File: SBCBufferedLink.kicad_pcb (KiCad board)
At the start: 2 copper layers, 9 parts, among them J1 Left, J2 Right

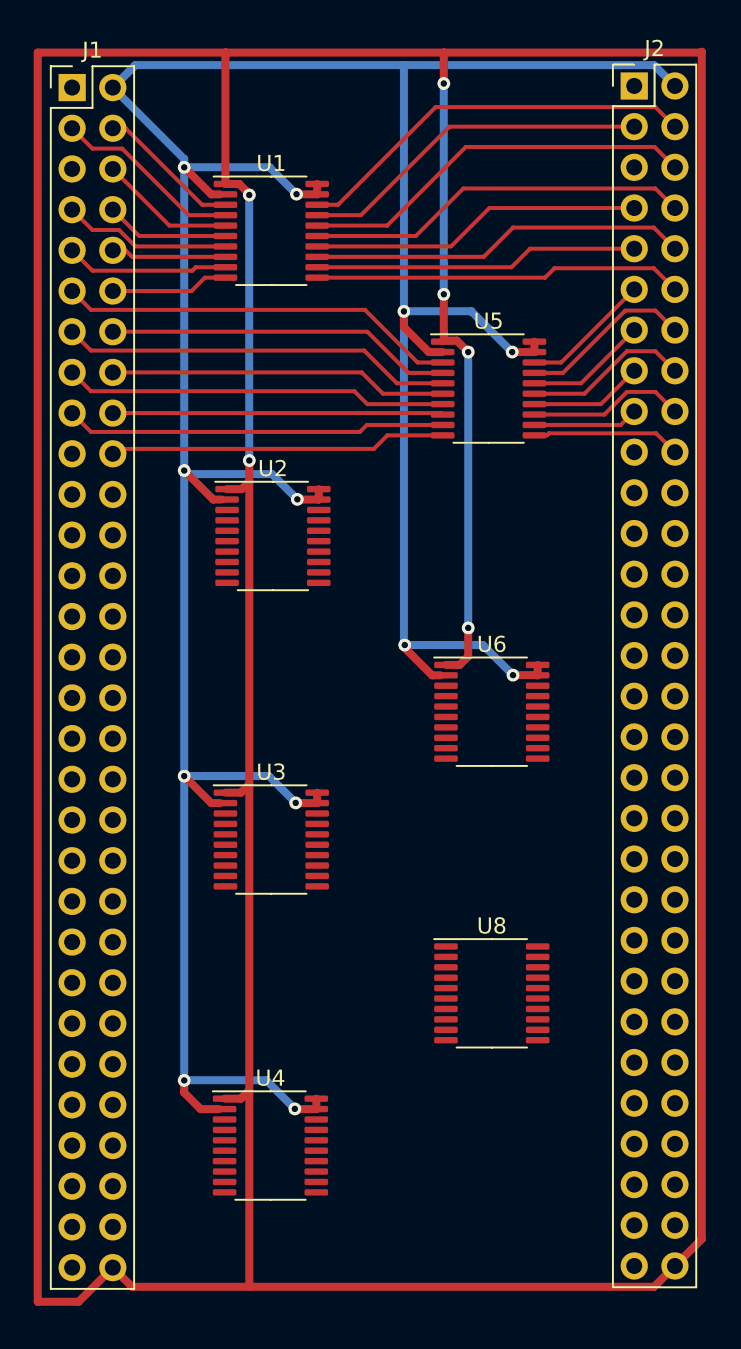
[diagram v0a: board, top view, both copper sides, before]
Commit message: add board edge
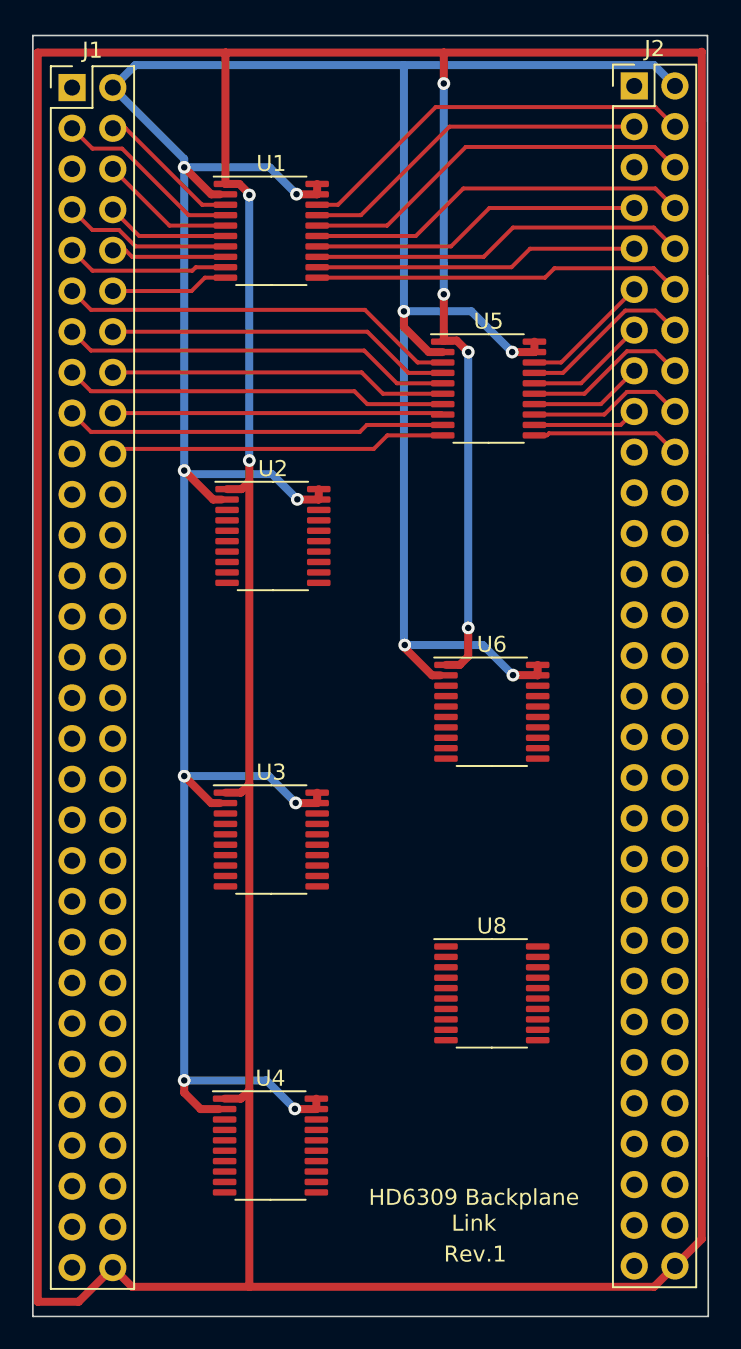
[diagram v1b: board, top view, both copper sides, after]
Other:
- board outline added: 42.2 x 80 mm
- board text added: "HD6309 Backplane Link"
- board text added: "Rev.1"
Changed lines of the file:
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@@
   )
   (paper "A4")
+  (title_block
+    (title "HD6309 SBC Backplane Link")
+    (date "2023-04-24")
+    (rev "Revision 1")
+  )
   (layers
     (0 "F.Cu" signal)
@@
     )
   )
+  (gr_line (start 107.2388 37.7952) (end 149.352 37.7952)
+    (stroke (width 0.1) (type default)) (layer "Edge.Cuts"))
+  (gr_line (start 107.2388 117.7544) (end 107.2388 37.7952)
+    (stroke (width 0.1) (type default)) (layer "Edge.Cuts"))
+  (gr_line (start 149.4028 117.7544) (end 107.2388 117.7544)
+    (stroke (width 0.1) (type default)) (layer "Edge.Cuts"))
+  (gr_line (start 149.352 37.7952) (end 149.4028 117.7544)
+    (stroke (width 0.1) (type default)) (layer "Edge.Cuts"))
   (gr_line (start 107.2896 60.0456) (end 149.7076 60.0456)
     (stroke (width 0.15) (type default)) (layer "User.1"))
@@
   (gr_line (start 122.174 34.544) (end 122.174 121.412)
     (stroke (width 0.15) (type default)) (layer "User.1"))
+  (gr_text "HD6309 Backplane\nLink" (at 134.7724 112.522) (layer "F.SilkS")
+    (effects (font (size 1 1) (thickness 0.15)) (justify bottom))
+  )
+  (gr_text "Rev.1" (at 132.8928 114.4524) (layer "F.SilkS")
+    (effects (font (size 1 1) (thickness 0.15)) (justify left bottom))
+  )
   (segment (start 123.709 47.7122) (end 124.9857 47.7122) (width 0.5) (layer "F.Cu") (net 2))
   (segment (start 118.375 47.7122) (end 118.920751 47.7122) (width 0.5) (layer "F.Cu") (net 2))

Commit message: complete tracing
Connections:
- J1 pad 44: unconnected-(J1-Pin_44-Pad44) -> NC1_LEFT
- J1 pad 53: unconnected-(J1-Pin_53-Pad53) -> NC2_LEFT
- J1 pad 57: unconnected-(J1-Pin_57-Pad57) -> NC3_LEFT
- J1 pad 58: unconnected-(J1-Pin_58-Pad58) -> NC4_LEFT
- J1 pad 59: unconnected-(J1-Pin_59-Pad59) -> NC5_LEFT
- J2 pad 44: unconnected-(J2-Pin_44-Pad44) -> NC1
- J2 pad 53: unconnected-(J2-Pin_53-Pad53) -> NC2
- J2 pad 57: unconnected-(J2-Pin_57-Pad57) -> NC3
- J2 pad 58: unconnected-(J2-Pin_58-Pad58) -> NC4
- J2 pad 59: unconnected-(J2-Pin_59-Pad59) -> NC5
- U2 pad 10: unconnected-(U2-A8-Pad10) -> A8_LEFT
- U2 pad 11: unconnected-(U2-B8-Pad11) -> A8
- U2 pad 12: unconnected-(U2-B7-Pad12) -> D7
- U2 pad 13: unconnected-(U2-B6-Pad13) -> A7
- U2 pad 14: unconnected-(U2-B5-Pad14) -> D6
- U2 pad 15: unconnected-(U2-B4-Pad15) -> A6
- U2 pad 16: unconnected-(U2-B3-Pad16) -> D5
- U2 pad 17: unconnected-(U2-B2-Pad17) -> A5
- U2 pad 18: unconnected-(U2-B1-Pad18) -> D4
- U2 pad 3: unconnected-(U2-A1-Pad3) -> D4_LEFT
- U2 pad 4: unconnected-(U2-A2-Pad4) -> A5_LEFT
- U2 pad 5: unconnected-(U2-A3-Pad5) -> D5_LEFT
- U2 pad 6: unconnected-(U2-A4-Pad6) -> A6_LEFT
- U2 pad 7: unconnected-(U2-A5-Pad7) -> D6_LEFT
- U2 pad 8: unconnected-(U2-A6-Pad8) -> A7_LEFT
- U2 pad 9: unconnected-(U2-A7-Pad9) -> D7_LEFT
- U3 pad 10: unconnected-(U3-A8-Pad10) -> NC1_LEFT
- U3 pad 11: unconnected-(U3-B8-Pad11) -> NC1
- U3 pad 12: unconnected-(U3-B7-Pad12) -> Q6
- U3 pad 13: unconnected-(U3-B6-Pad13) -> A15
- U3 pad 14: unconnected-(U3-B5-Pad14) -> Q5
- U3 pad 15: unconnected-(U3-B4-Pad15) -> A14
- U3 pad 16: unconnected-(U3-B3-Pad16) -> Q4
- U3 pad 17: unconnected-(U3-B2-Pad17) -> A13
- U3 pad 18: unconnected-(U3-B1-Pad18) -> Q3
- U3 pad 3: unconnected-(U3-A1-Pad3) -> Q3_LEFT
- U3 pad 4: unconnected-(U3-A2-Pad4) -> A13_LEFT
- U3 pad 5: unconnected-(U3-A3-Pad5) -> Q4_LEFT
- U3 pad 6: unconnected-(U3-A4-Pad6) -> A14_LEFT
- U3 pad 7: unconnected-(U3-A5-Pad7) -> Q5_LEFT
- U3 pad 8: unconnected-(U3-A6-Pad8) -> A15_LEFT
- U3 pad 9: unconnected-(U3-A7-Pad9) -> Q6_LEFT
- U4 pad 10: unconnected-(U4-A8-Pad10) -> NC5_LEFT
- U4 pad 11: unconnected-(U4-B8-Pad11) -> NC5
- U4 pad 12: unconnected-(U4-B7-Pad12) -> NC3
- U4 pad 13: unconnected-(U4-B6-Pad13) -> NC4
- U4 pad 14: unconnected-(U4-B5-Pad14) -> MRDY
- U4 pad 15: unconnected-(U4-B4-Pad15) -> BS
- U4 pad 16: unconnected-(U4-B3-Pad16) -> NC2
- U4 pad 17: unconnected-(U4-B2-Pad17) -> BA
- U4 pad 18: unconnected-(U4-B1-Pad18) -> ~{HALT}
- U4 pad 3: unconnected-(U4-A1-Pad3) -> ~{HALT}_LEFT
- U4 pad 4: unconnected-(U4-A2-Pad4) -> BA_LEFT
- U4 pad 5: unconnected-(U4-A3-Pad5) -> NC2_LEFT
- U4 pad 6: unconnected-(U4-A4-Pad6) -> BS_LEFT
- U4 pad 7: unconnected-(U4-A5-Pad7) -> MRDY_LEFT
- U4 pad 8: unconnected-(U4-A6-Pad8) -> NC4_LEFT
- U4 pad 9: unconnected-(U4-A7-Pad9) -> NC3_LEFT
- U6 pad 10: unconnected-(U6-A8-Pad10) -> A12_LEFT
- U6 pad 11: unconnected-(U6-B8-Pad11) -> A12
- U6 pad 12: unconnected-(U6-B7-Pad12) -> Q2
- U6 pad 13: unconnected-(U6-B6-Pad13) -> A11
- U6 pad 14: unconnected-(U6-B5-Pad14) -> Q1
- U6 pad 15: unconnected-(U6-B4-Pad15) -> A10
- U6 pad 16: unconnected-(U6-B3-Pad16) -> ROM/~{RAM}
- U6 pad 17: unconnected-(U6-B2-Pad17) -> A9
- U6 pad 18: unconnected-(U6-B1-Pad18) -> MAPPED_MEM
- U6 pad 3: unconnected-(U6-A1-Pad3) -> MAPPED_MEM_LEFT
- U6 pad 4: unconnected-(U6-A2-Pad4) -> A9_LEFT
- U6 pad 5: unconnected-(U6-A3-Pad5) -> ROM/~{RAM}_LEFT
- U6 pad 6: unconnected-(U6-A4-Pad6) -> A10_LEFT
- U6 pad 7: unconnected-(U6-A5-Pad7) -> Q1_LEFT
- U6 pad 8: unconnected-(U6-A6-Pad8) -> A11_LEFT
- U6 pad 9: unconnected-(U6-A7-Pad9) -> Q2_LEFT
- U8 pad 10: unconnected-(U8-A8-Pad10) -> ~{IRQ}_LEFT
- U8 pad 11: unconnected-(U8-B8-Pad11) -> ~{IRQ}
- U8 pad 12: unconnected-(U8-B7-Pad12) -> R/~{W}
- U8 pad 13: unconnected-(U8-B6-Pad13) -> ~{FIRQ}
- U8 pad 14: unconnected-(U8-B5-Pad14) -> ~{DMA}
- U8 pad 15: unconnected-(U8-B4-Pad15) -> ~{NMI}
- U8 pad 16: unconnected-(U8-B3-Pad16) -> Q8
- U8 pad 17: unconnected-(U8-B2-Pad17) -> ~{RESET}
- U8 pad 18: unconnected-(U8-B1-Pad18) -> Q7
- U8 pad 3: unconnected-(U8-A1-Pad3) -> Q7_LEFT
- U8 pad 4: unconnected-(U8-A2-Pad4) -> ~{RESET}_LEFT
- U8 pad 5: unconnected-(U8-A3-Pad5) -> Q8_LEFT
- U8 pad 6: unconnected-(U8-A4-Pad6) -> ~{NMI}_LEFT
- U8 pad 7: unconnected-(U8-A5-Pad7) -> ~{DMA}_LEFT
- U8 pad 8: unconnected-(U8-A6-Pad8) -> ~{FIRQ}_LEFT
- U8 pad 9: unconnected-(U8-A7-Pad9) -> R/~{W}_LEFT
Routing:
- net +5V: track 214.1 -> 245.3 mm, vias 12 -> 14
- net R/~{W}_LEFT: track 0.00 -> 25.3 mm
- net MAPPED_MEM_LEFT: track 0.00 -> 25.1 mm
- net ~{DMA}_LEFT: track 0.00 -> 24.7 mm
- net Q2_LEFT: track 0.00 -> 24.7 mm
- net ROM/~{RAM}_LEFT: track 0.00 -> 24.6 mm
- net Q8_LEFT: track 0.00 -> 24.2 mm
- net Q1_LEFT: track 0.00 -> 24.1 mm
- net Q7_LEFT: track 0.00 -> 24.0 mm
- net A5: track 0.00 -> 23.9 mm
- net NC4: track 0.00 -> 23.8 mm
- net NC1: track 0.00 -> 23.7 mm
- net A13: track 0.00 -> 23.5 mm
- net A6: track 0.00 -> 23.4 mm
- net BS: track 0.00 -> 23.3 mm
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- added copper zone on B.Cu, net GND
- added copper zone on F.Cu, net GND
